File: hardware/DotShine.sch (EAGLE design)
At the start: 56 parts, among them CN1 1X4-BIG, IC1 CAT24M010TS, IC3 SI1145, J3 USB-MICROB, U1 ATMEGA328P-MU-QFN32, U2 TMP102, U3 ATSHA204-TSU, X2 MC-RTC-RV-4162-C7-I2C, X3 S4B-ZR

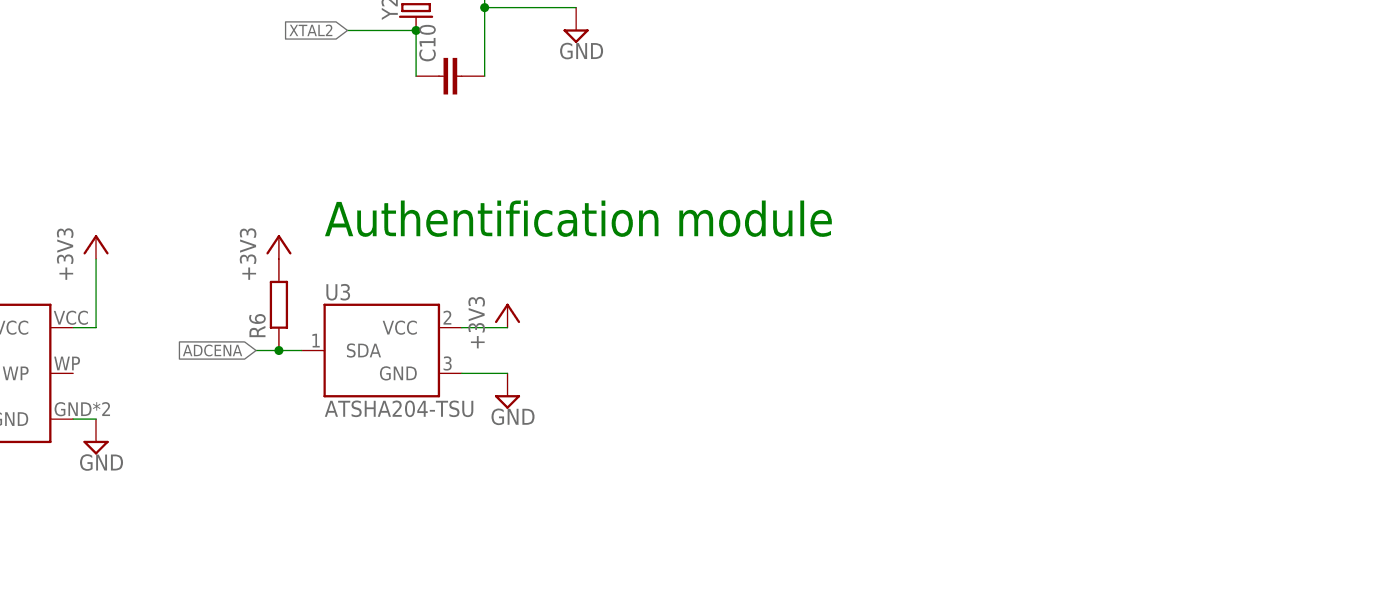
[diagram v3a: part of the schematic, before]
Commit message: Add SJ for ADCENA and RST -> HW reset through SW
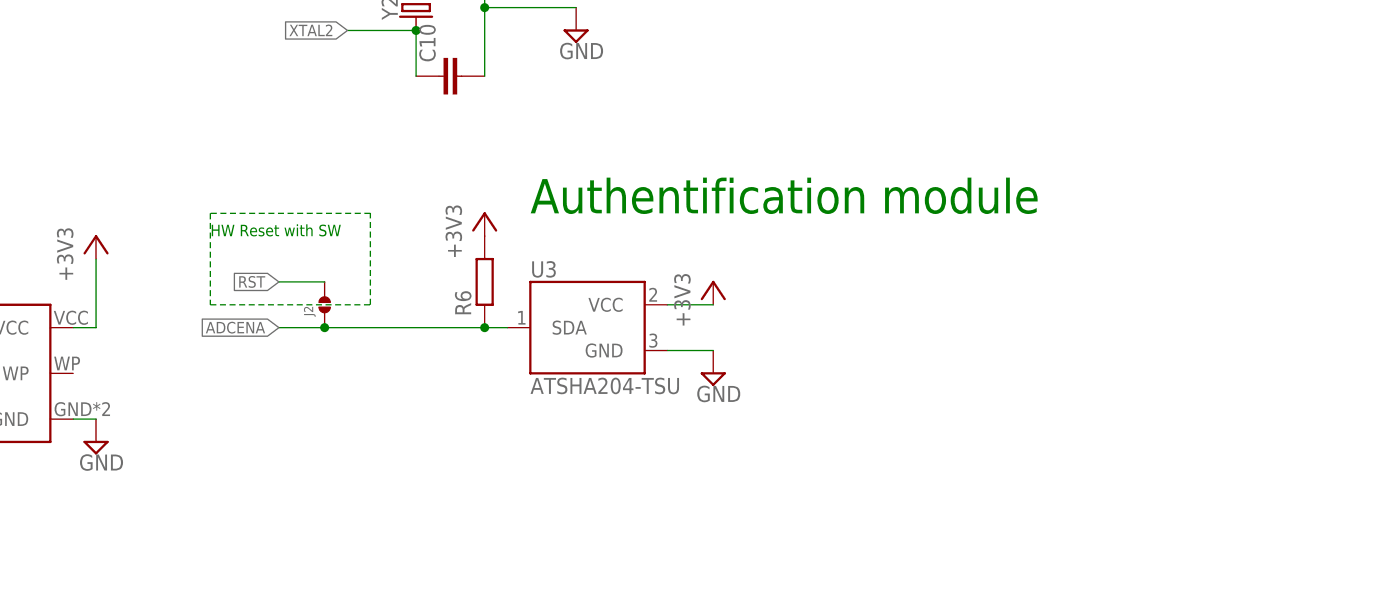
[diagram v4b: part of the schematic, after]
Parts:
- added J2: (no value), solderjumper:SOLDERJUMPER.2.MED
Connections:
- net ADCENA: now also J2.1
- net RST: now also J2.2
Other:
- note added: "HW Reset with SW"
- moved on the sheet: R6, U3
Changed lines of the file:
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@@
 <setting verticaltext="up"/>
 </settings>
-<grid distance="0.05" unitdist="inch" unit="inch" style="lines" multiple="1" display="no" altdistance="0.01" altunitdist="inch" altunit="inch"/>
+<grid distance="0.1" unitdist="inch" unit="inch" style="lines" multiple="1" display="no" altdistance="0.01" altunitdist="inch" altunit="inch"/>
 <layers>
 <layer number="1" name="Top" color="4" fill="1" visible="no" active="no"/>
@@
 <part name="LED7" library="SparkFun" deviceset="LED" device="0603"/>
 <part name="+3V3" library="supply1" deviceset="+3V3" device=""/>
+<part name="J2" library="solderjumper" deviceset="SOLDERJUMPER.2" device=".MED"/>
 </parts>
 <sheets>
@@
 <text x="-10.922" y="50.8" size="1.27" layer="91">Red</text>
 <text x="228.6" y="20.32" size="1.016" layer="91" align="center">TMP102 or TMP112 (high acc +/-0.5°)</text>
-<text x="137.16" y="-147.32" size="3.81" layer="91">Authentification module</text>
+<text x="160.02" y="-144.78" size="3.81" layer="91">Authentification module</text>
 <text x="134.62" y="134.62" size="1.778" layer="91">white</text>
 <text x="134.62" y="124.46" size="1.778" layer="91">red</text>
@@
 <text x="248.92" y="-71.12" size="1.778" layer="91">5V Zener, otherwise
 leakage current too high </text>
+<text x="124.46" y="-147.32" size="1.27" layer="91">HW Reset with SW</text>
 </plain>
 <instances>
@@
 <instance part="IC1" gate="G$1" x="93.98" y="-162.56"/>
 <instance part="+3V9" gate="G$1" x="111.76" y="-147.32"/>
-<instance part="U3" gate="G$1" x="144.78" y="-160.02"/>
-<instance part="+3V10" gate="G$1" x="157.48" y="-154.94"/>
-<instance part="SUPPLY18" gate="GND" x="157.48" y="-165.1"/>
-<instance part="R6" gate="G$1" x="132.08" y="-154.94" rot="R90"/>
-<instance part="+3V13" gate="G$1" x="132.08" y="-147.32"/>
+<instance part="U3" gate="G$1" x="167.64" y="-157.48"/>
+<instance part="+3V10" gate="G$1" x="180.34" y="-152.4"/>
+<instance part="SUPPLY18" gate="GND" x="180.34" y="-162.56"/>
+<instance part="R6" gate="G$1" x="154.94" y="-152.4" rot="R90"/>
+<instance part="+3V13" gate="G$1" x="154.94" y="-144.78"/>
 <instance part="C2" gate="G$1" x="142.24" y="-88.9" rot="R180"/>
 <instance part="+3V15" gate="G$1" x="142.24" y="-81.28"/>
@@
 <instance part="LED7" gate="G$1" x="132.08" y="152.4" rot="R270"/>
 <instance part="+3V3" gate="G$1" x="46.99" y="-205.74"/>
+<instance part="J2" gate="G$1" x="137.16" y="-154.94" rot="R90"/>
 </instances>
 <busses>
@@
 <segment>
 <pinref part="U3" gate="G$1" pin="GND"/>
-<wire x1="152.4" y1="-162.56" x2="157.48" y2="-162.56" width="0.1524" layer="91"/>
+<wire x1="175.26" y1="-160.02" x2="180.34" y2="-160.02" width="0.1524" layer="91"/>
 <pinref part="SUPPLY18" gate="GND" pin="GND"/>
 </segment>
@@
 <wire x1="127" y1="152.4" x2="123.19" y2="152.4" width="0.1524" layer="91"/>
 <label x="123.19" y="152.4" size="1.778" layer="95" rot="R180" xref="yes"/>
+</segment>
+<segment>
+<pinref part="J2" gate="G$1" pin="2"/>
+<wire x1="137.16" y1="-152.4" x2="132.08" y2="-152.4" width="0.1524" layer="91"/>
+<label x="132.08" y="-152.4" size="1.27" layer="95" rot="R180" xref="yes"/>
 </segment>
 </net>
@@
 <segment>
 <pinref part="U3" gate="G$1" pin="VCC"/>
-<wire x1="152.4" y1="-157.48" x2="157.48" y2="-157.48" width="0.1524" layer="91"/>
+<wire x1="175.26" y1="-154.94" x2="180.34" y2="-154.94" width="0.1524" layer="91"/>
 <pinref part="+3V10" gate="G$1" pin="+3V3"/>
 </segment>
@@
 <segment>
 <pinref part="U3" gate="G$1" pin="SDA"/>
-<wire x1="134.62" y1="-160.02" x2="132.08" y2="-160.02" width="0.1524" layer="91"/>
-<label x="129.54" y="-160.02" size="1.27" layer="95" rot="R180" xref="yes"/>
+<wire x1="157.48" y1="-157.48" x2="154.94" y2="-157.48" width="0.1524" layer="91"/>
+<label x="132.08" y="-157.48" size="1.27" layer="95" rot="R180" xref="yes"/>
 <pinref part="R6" gate="G$1" pin="1"/>
-<wire x1="132.08" y1="-160.02" x2="129.54" y2="-160.02" width="0.1524" layer="91"/>
-<junction x="132.08" y="-160.02"/>
+<wire x1="154.94" y1="-157.48" x2="137.16" y2="-157.48" width="0.1524" layer="91"/>
+<junction x="154.94" y="-157.48"/>
+<pinref part="J2" gate="G$1" pin="1"/>
+<wire x1="137.16" y1="-157.48" x2="132.08" y2="-157.48" width="0.1524" layer="91"/>
+<junction x="137.16" y="-157.48"/>
 </segment>
 <segment>
@@
 </segment>
 </net>
+<net name="N$12" class="0">
+<segment>
+<wire x1="142.24" y1="-144.78" x2="124.46" y2="-144.78" width="0.1524" layer="91" style="shortdash"/>
+<wire x1="124.46" y1="-144.78" x2="124.46" y2="-154.94" width="0.1524" layer="91" style="shortdash"/>
+<wire x1="124.46" y1="-154.94" x2="142.24" y2="-154.94" width="0.1524" layer="91" style="shortdash"/>
+<wire x1="142.24" y1="-154.94" x2="142.24" y2="-144.78" width="0.1524" layer="91" style="shortdash"/>
+</segment>
+</net>

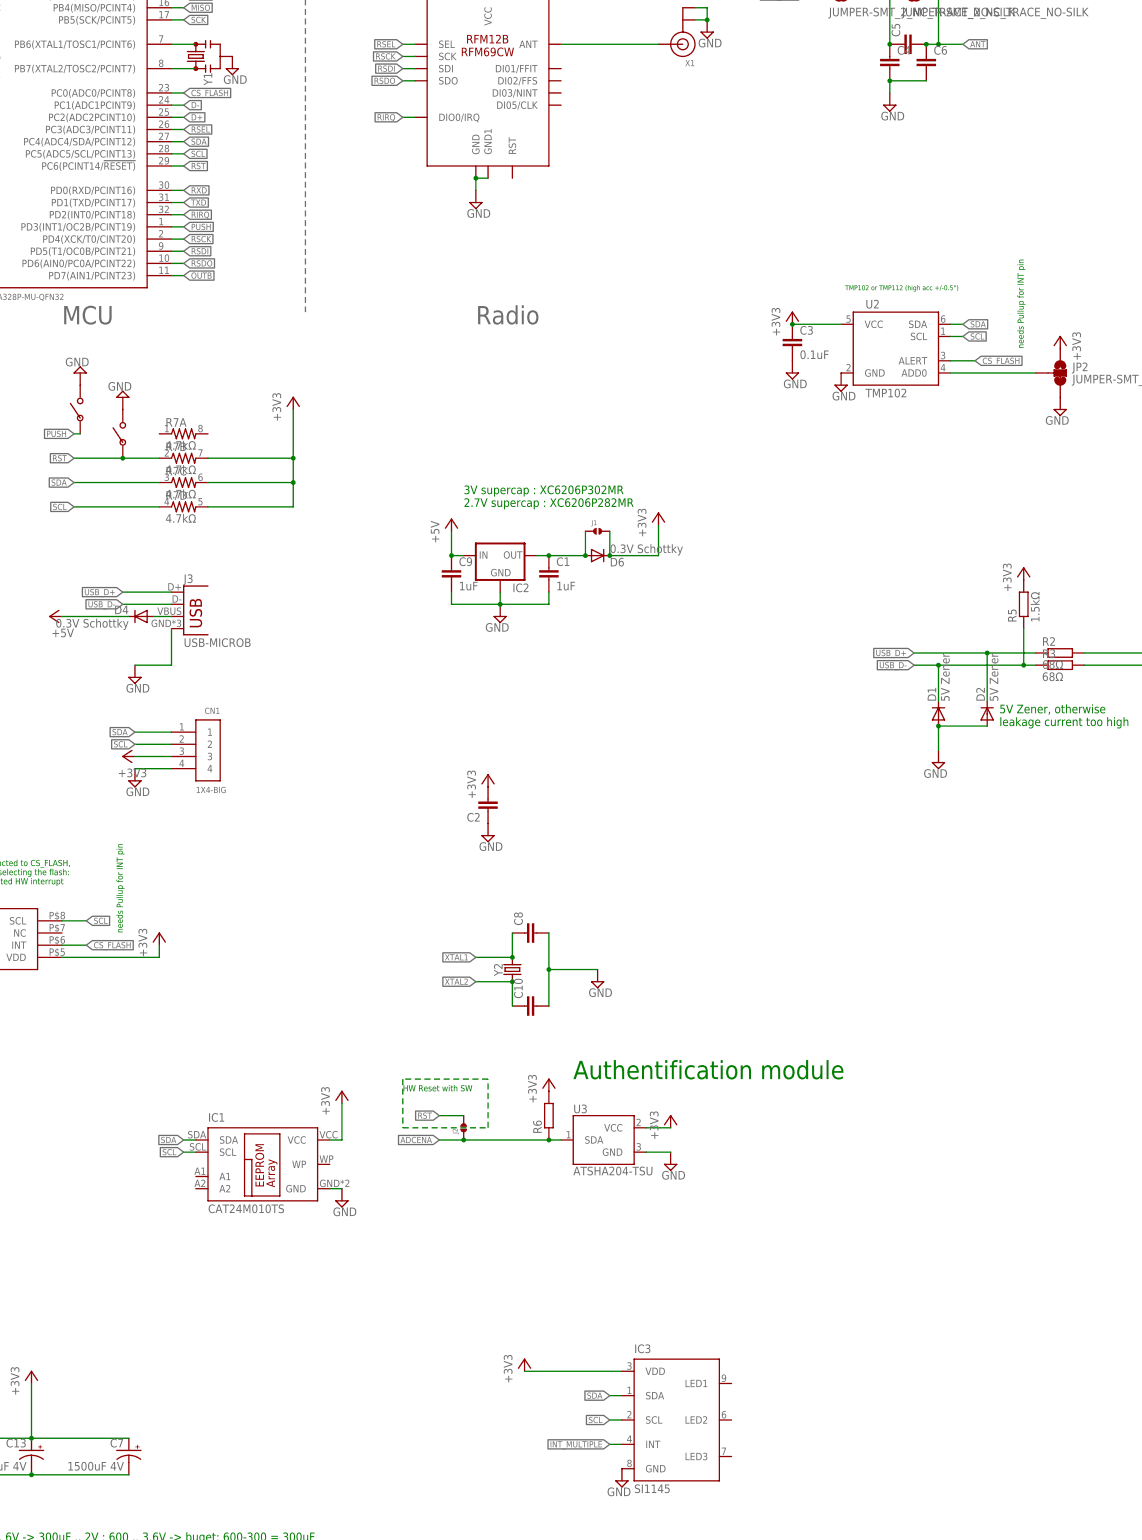
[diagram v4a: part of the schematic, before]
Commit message: Add UV Sensor INT to cabled OR
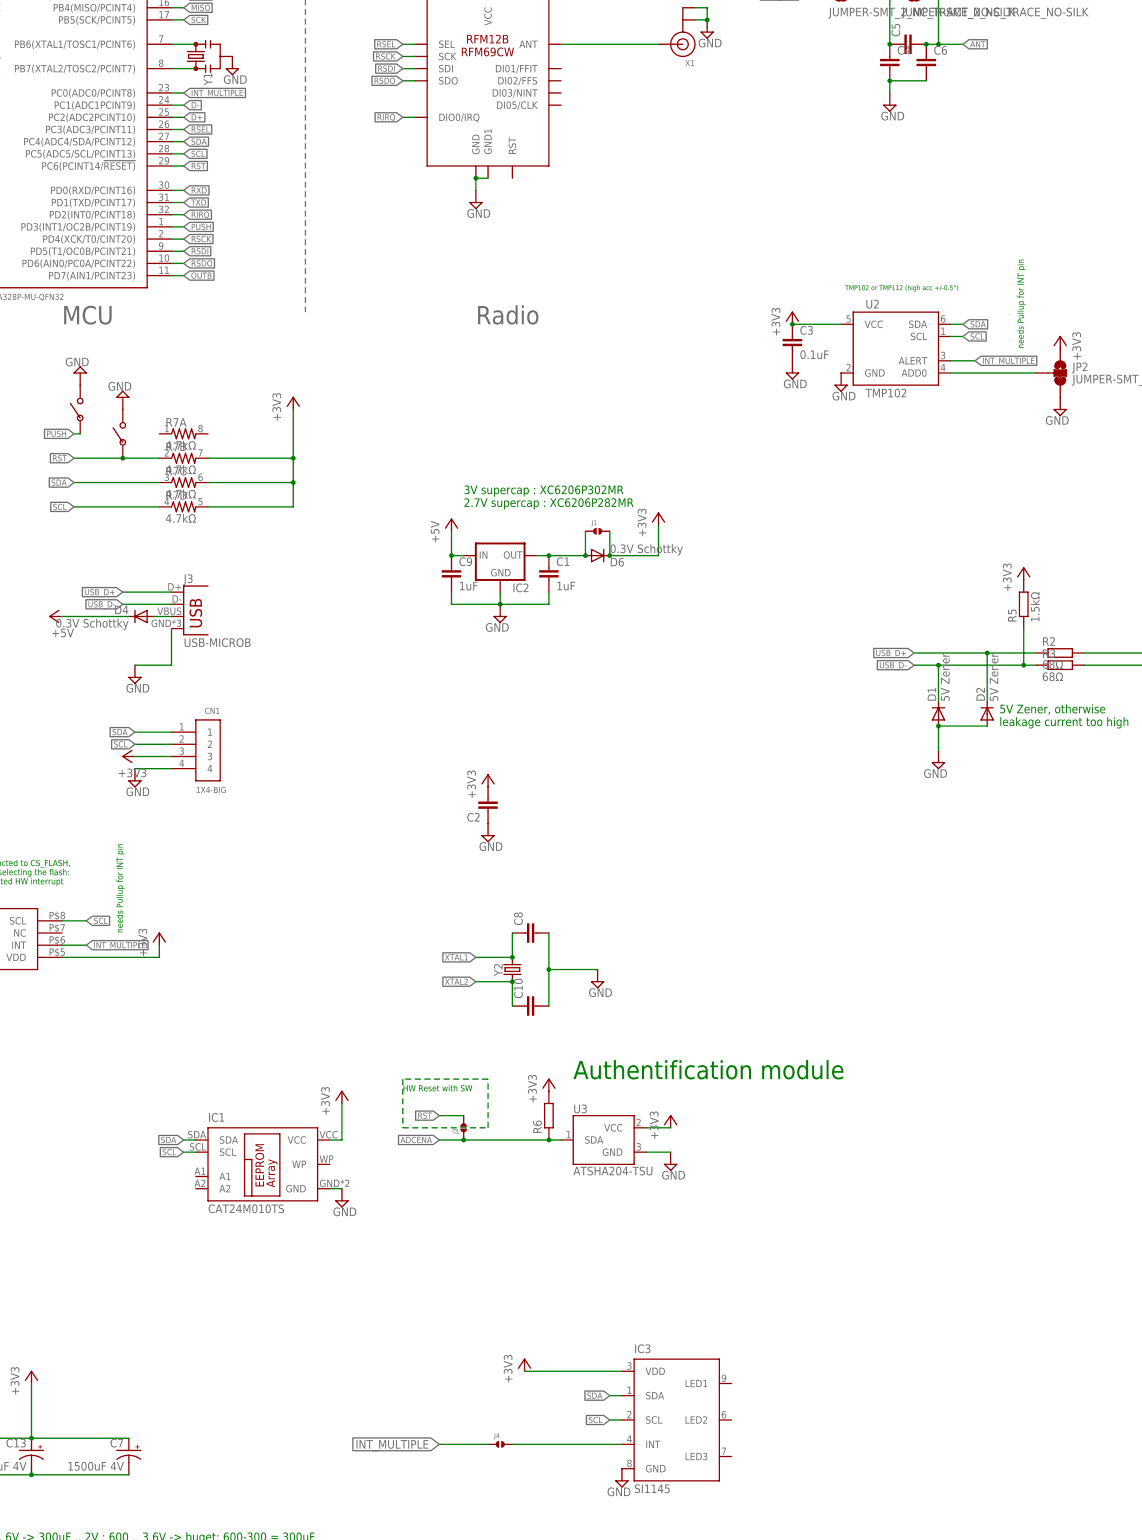
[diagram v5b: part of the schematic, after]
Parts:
- added J4: (no value), solderjumper:SOLDERJUMPER.2.MED
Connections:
- removed net CS_FLASH: U1.PC0(ADC0/PCINT8), U2.ALERT, X2.INT
- new net N$33: IC3.INT, J4.2
- net INT_MULTIPLE: now also J4.1, U1.PC0(ADC0/PCINT8), U2.ALERT, X2.INT; no longer IC3.INT
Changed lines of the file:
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@@
 <part name="+3V3" library="supply1" deviceset="+3V3" device=""/>
 <part name="J2" library="solderjumper" deviceset="SOLDERJUMPER.2" device=".MED"/>
+<part name="J4" library="solderjumper" deviceset="SOLDERJUMPER.2" device=".MED"/>
 </parts>
 <sheets>
@@
 <instance part="+3V3" gate="G$1" x="46.99" y="-205.74"/>
 <instance part="J2" gate="G$1" x="137.16" y="-154.94" rot="R90"/>
+<instance part="J4" gate="G$1" x="144.78" y="-220.98"/>
 </instances>
 <busses>
@@
 </segment>
 </net>
-<net name="CS_FLASH" class="0">
-<segment>
-<pinref part="U1" gate="G$1" pin="PC0(ADC0/PCINT8)"/>
-<wire x1="76.2" y1="60.96" x2="78.74" y2="60.96" width="0.1524" layer="91"/>
-<label x="78.74" y="60.96" size="1.27" layer="95" xref="yes"/>
-</segment>
-<segment>
-<pinref part="X2" gate="G$1" pin="INT"/>
-<wire x1="53.34" y1="-116.84" x2="58.42" y2="-116.84" width="0.1524" layer="91"/>
-<label x="58.42" y="-116.84" size="1.27" layer="95" xref="yes"/>
-</segment>
-<segment>
-<label x="243.84" y="5.08" size="1.27" layer="95" xref="yes"/>
-<pinref part="U2" gate="G$1" pin="ALERT"/>
-<wire x1="238.76" y1="5.08" x2="243.84" y2="5.08" width="0.1524" layer="91"/>
-</segment>
-</net>
 <net name="N$13" class="0">
 <segment>
@@
 <pinref part="D5" gate="G$1" pin="A"/>
 <wire x1="-15.24" y1="-209.55" x2="-7.62" y2="-209.55" width="0.1524" layer="91"/>
-</segment>
-</net>
-<net name="INT_MULTIPLE" class="0">
-<segment>
-<pinref part="IC3" gate="G$1" pin="INT"/>
-<wire x1="170.18" y1="-220.98" x2="167.64" y2="-220.98" width="0.1524" layer="91"/>
-<label x="167.64" y="-220.98" size="1.27" layer="95" rot="R180" xref="yes"/>
 </segment>
 </net>
@@
 </segment>
 </net>
+<net name="N$33" class="0">
+<segment>
+<pinref part="IC3" gate="G$1" pin="INT"/>
+<pinref part="J4" gate="G$1" pin="2"/>
+<wire x1="170.18" y1="-220.98" x2="147.32" y2="-220.98" width="0.1524" layer="91"/>
+</segment>
+</net>
+<net name="INT_MULTIPLE" class="0">
+<segment>
+<pinref part="J4" gate="G$1" pin="1"/>
+<wire x1="142.24" y1="-220.98" x2="132.08" y2="-220.98" width="0.1524" layer="91"/>
+<label x="132.08" y="-220.98" size="1.778" layer="95" rot="R180" xref="yes"/>
+</segment>
+<segment>
+<pinref part="X2" gate="G$1" pin="INT"/>
+<wire x1="53.34" y1="-116.84" x2="58.42" y2="-116.84" width="0.1524" layer="91"/>
+<label x="58.42" y="-116.84" size="1.27" layer="95" xref="yes"/>
+</segment>
+<segment>
+<label x="243.84" y="5.08" size="1.27" layer="95" xref="yes"/>
+<pinref part="U2" gate="G$1" pin="ALERT"/>
+<wire x1="238.76" y1="5.08" x2="243.84" y2="5.08" width="0.1524" layer="91"/>
+</segment>
+<segment>
+<pinref part="U1" gate="G$1" pin="PC0(ADC0/PCINT8)"/>
+<wire x1="76.2" y1="60.96" x2="78.74" y2="60.96" width="0.1524" layer="91"/>
+<label x="78.74" y="60.96" size="1.27" layer="95" xref="yes"/>
+</segment>
+</net>

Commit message: UV power controlled from MCU (no sleep), TXD to JST
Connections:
- removed net N$1: LED1.CBLUE, R1B.2
- removed net N$2: LED3.C, R4A.1
- removed net OUTA: LED3.A, U1.PB2(SS/OC1B/PCINT2), X3-3.1
- removed net OUTB: LED4.A, U1.PD7(AIN1/PCINT23), X3-2.1
- new net OUTAB: R4A.2, U1.PB2(SS/OC1B/PCINT2), X3-3.1
- new net TXD_OUT: LED1.CBLUE, R1B.2, X3-2.1
- new net UV_ON: IC3.VDD, U1.PD7(AIN1/PCINT23)
- net +3V3: now also LED3.A; no longer IC3.VDD
- net GND: now also LED4.C; no longer R4A.2, R4B.2
- net N$9: now also LED3.C, LED4.A, R4A.1; no longer LED4.C, R4B.1
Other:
- moved on the sheet: LED2, LED3, LED4, LED7, R4A, R4B
